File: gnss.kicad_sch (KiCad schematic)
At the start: 72 parts, among them J11 SMA-KE-347-H13.5-1.6, J12 U.FL, SW4 RESET_GNSS, SW5 SAFEBOOT_GNSS, U10 TPS7A2033PDBVR, U11 TPS259474LRPWR, U6 TPS22945DCKR, U9 NEO-F10N

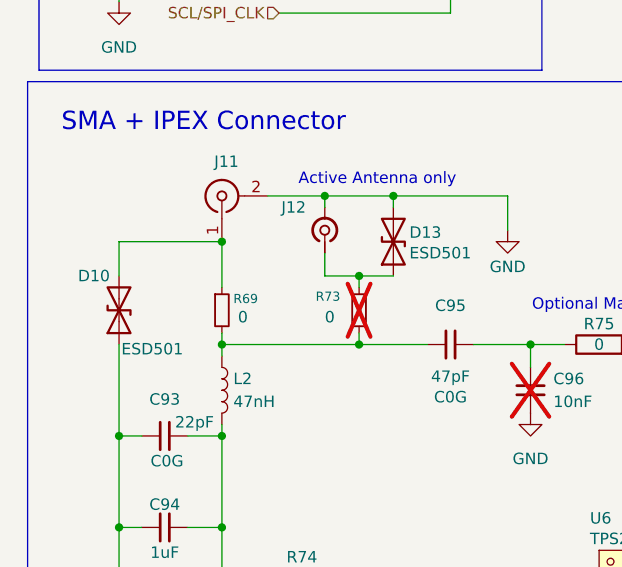
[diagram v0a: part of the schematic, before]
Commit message: Netclasses: label the classed nets, add missing members
Netclass patterns keyed to KiCad's refdes-derived names (Net-(D18-A2) etc.)
drop out of their class silently on re-annotation. Local labels now name 14
of those nets (sheets + board renamed together; connectivity unchanged).

- RF_50OHM: LoRa LPF in/out + SMA, GNSS SMA + bias node now by label.
- RF_50OHM_MS: GNSS_UFL by label; width 0.30 -> 0.34 mm (50 ohm at 0.8 mm
  side clearance; 0.30 solves to 53 ohm).
- PWR_HIGH: + CHG_VBUS, /Charger/SW1, SW2, CHG_BAT, VAC1_MID, /BMS/CELL_BOT,
  BMS FET mid (full pack / charge current, previously Default).
- PWR_RAIL: + buck switch nodes, LORA_5V (E22P supply), SOLAR, VAC2_MID,
  LED 5V connector feed.
- USB_DIFF: + the six USB data nets; clearance 0.20 -> 0.15 mm (FS USB,
  matches the routed pairs).
- Root-hierarchy patterns written as */Sheet/NAME: the GUI names these
  /Root/Sheet/NAME, kicad-cli parity /Sheet/NAME.
- 8 nets had no spot for a label clear of existing text; they keep their
  current name plus the intended label name as a second pattern.
- .dru unfused_pack_plus rule names /BMS/CELL_TOP and /BMS/CELL_BOT.

Verified: knet diff (renames only), refilled DRC and ERC identical to
before, kpcb sync clean.

Co-Authored-By: Claude Opus 5.5 <noreply@anthropic.com>
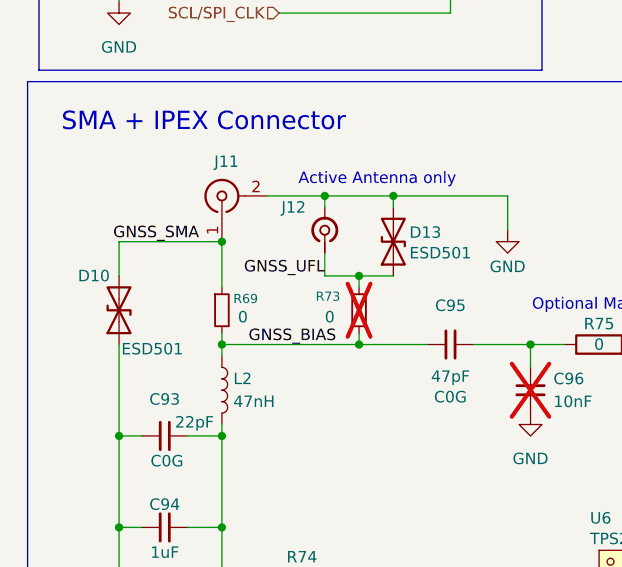
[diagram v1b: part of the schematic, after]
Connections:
- net GNSS_UFL: now reaches D13.1 (A1), J12.1 (In), R73.1
- net GNSS_BIAS: now reaches C95.2, L2.1, R69.2, R73.2
- net GNSS_SMA: now reaches D10.2 (A2), J11.1 (In), R69.1
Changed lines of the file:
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@@
+		)
+	)
+	(label "GNSS_UFL"
+		(at 46.99 137.16 180)
+		(effects
+			(font
+				(size 1.27 1.27)
+			)
+			(justify right bottom)
+		)
+	)
+	(label "GNSS_BIAS"
+		(at 48.26 144.78 180)
+		(effects
+			(font
+				(size 1.27 1.27)
+			)
+			(justify right bottom)
+		)
+	)
+	(label "GNSS_SMA"
+		(at 33.02 133.35 180)
+		(effects
+			(font
+				(size 1.27 1.27)
+			)
+			(justify right bottom)
 		)
 	)
